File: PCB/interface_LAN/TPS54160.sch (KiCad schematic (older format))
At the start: 17 parts, among them U22 TPS54160

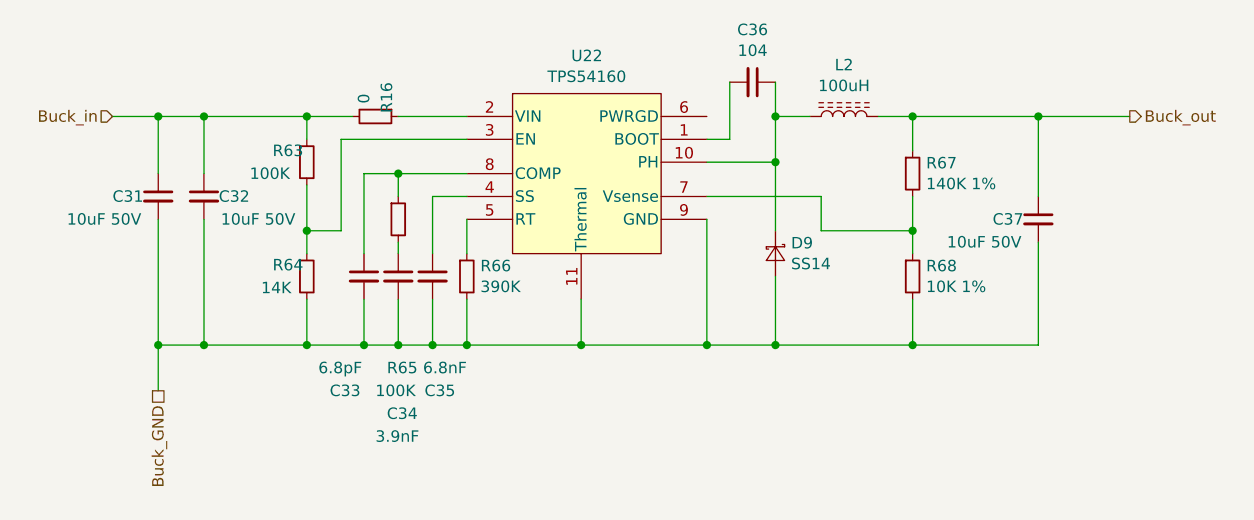
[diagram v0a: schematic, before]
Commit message: Implemented the ESP-IDF version. First passed compilation
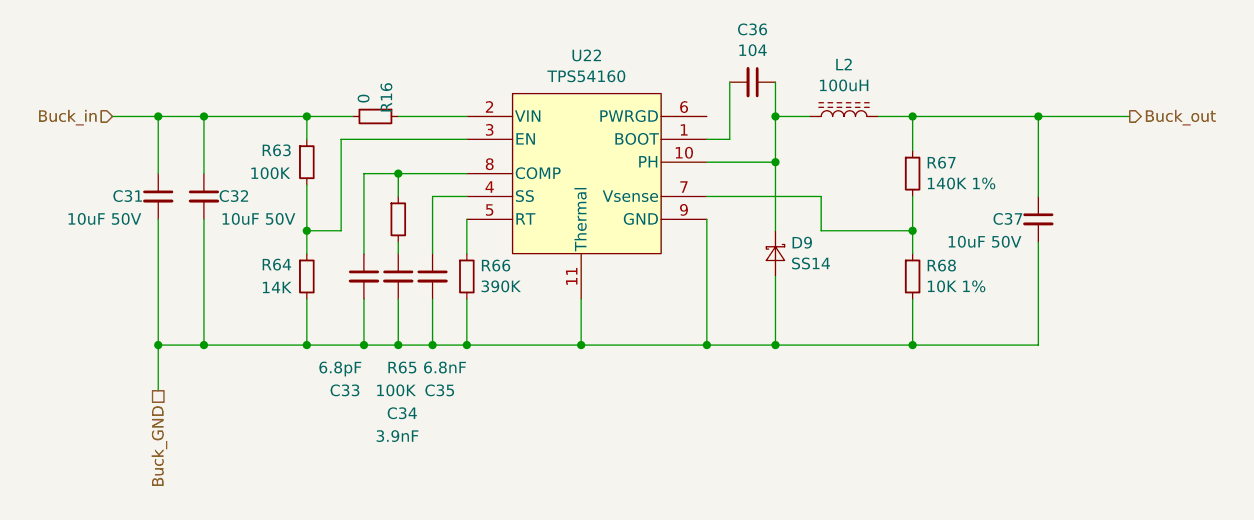
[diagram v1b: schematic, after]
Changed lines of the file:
@@
 AR Path="/63E76FBF/63F9B266" Ref="R?"  Part="1"
 AR Path="/63F91570/63F9B266" Ref="R63"  Part="1"
-F 0 "R63" H 3400 2600 50  0000 L CNN
+F 0 "R63" H 3350 2600 50  0000 L CNN
 F 1 "100K" H 3300 2500 50  0000 L CNN
 F 2 "lc_lib:0805_R" H 3550 2550 50  0001 C CNN
@@
 AR Path="/63E76FBF/63F9B26C" Ref="R?"  Part="1"
 AR Path="/63F91570/63F9B26C" Ref="R64"  Part="1"
-F 0 "R64" H 3400 3100 50  0000 L CNN
+F 0 "R64" H 3350 3100 50  0000 L CNN
 F 1 "14K" H 3350 3000 50  0000 L CNN
 F 2 "lc_lib:0805_R" H 3550 3050 50  0001 C CNN
